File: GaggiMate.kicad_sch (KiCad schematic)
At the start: 26 parts, among them J1 Heater SSR, J13 ESP out, J2 HV_VALVE, J3 K-Type probe, J4 Analog, J5 Pressure Sensor, J6 Brew BTN, J7 Steam BTN, J8 HV_PUMP, J9 HX711 connector, P1 USB_C_Plug_USB2.0, U1 ESP32-S3-WROOM-1, U2 MAX31855KASA, U3 ADS1115IDGS, U4 AMS1117-3.3

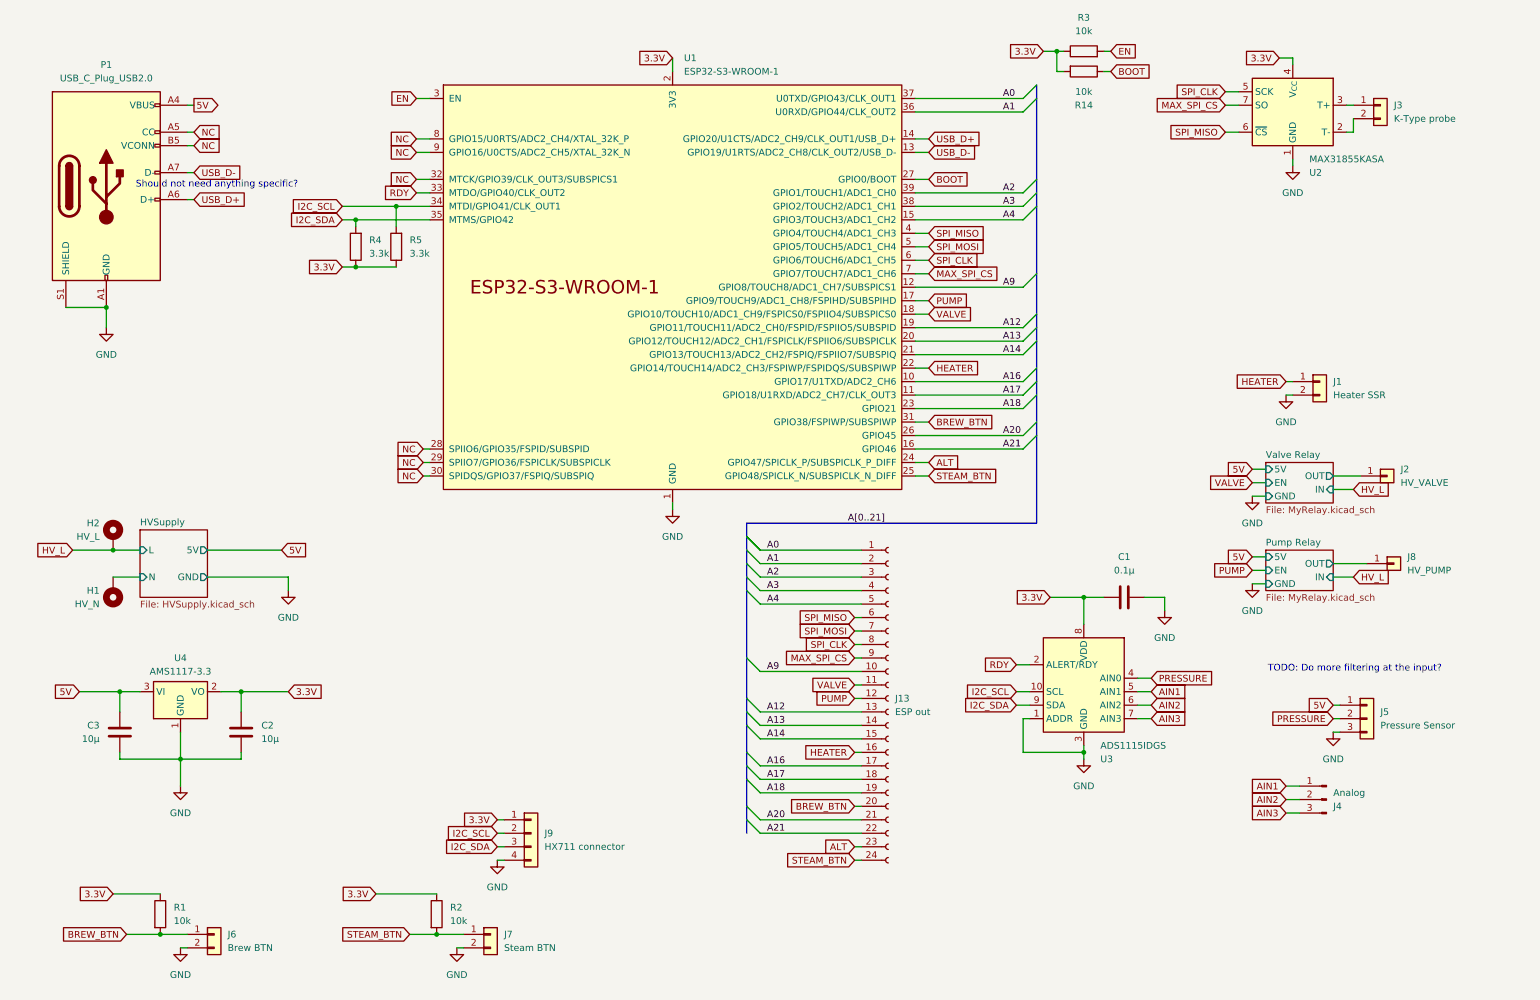
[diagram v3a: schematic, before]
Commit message: update footprints, add 230v module, use SSRs and do some basic layouting
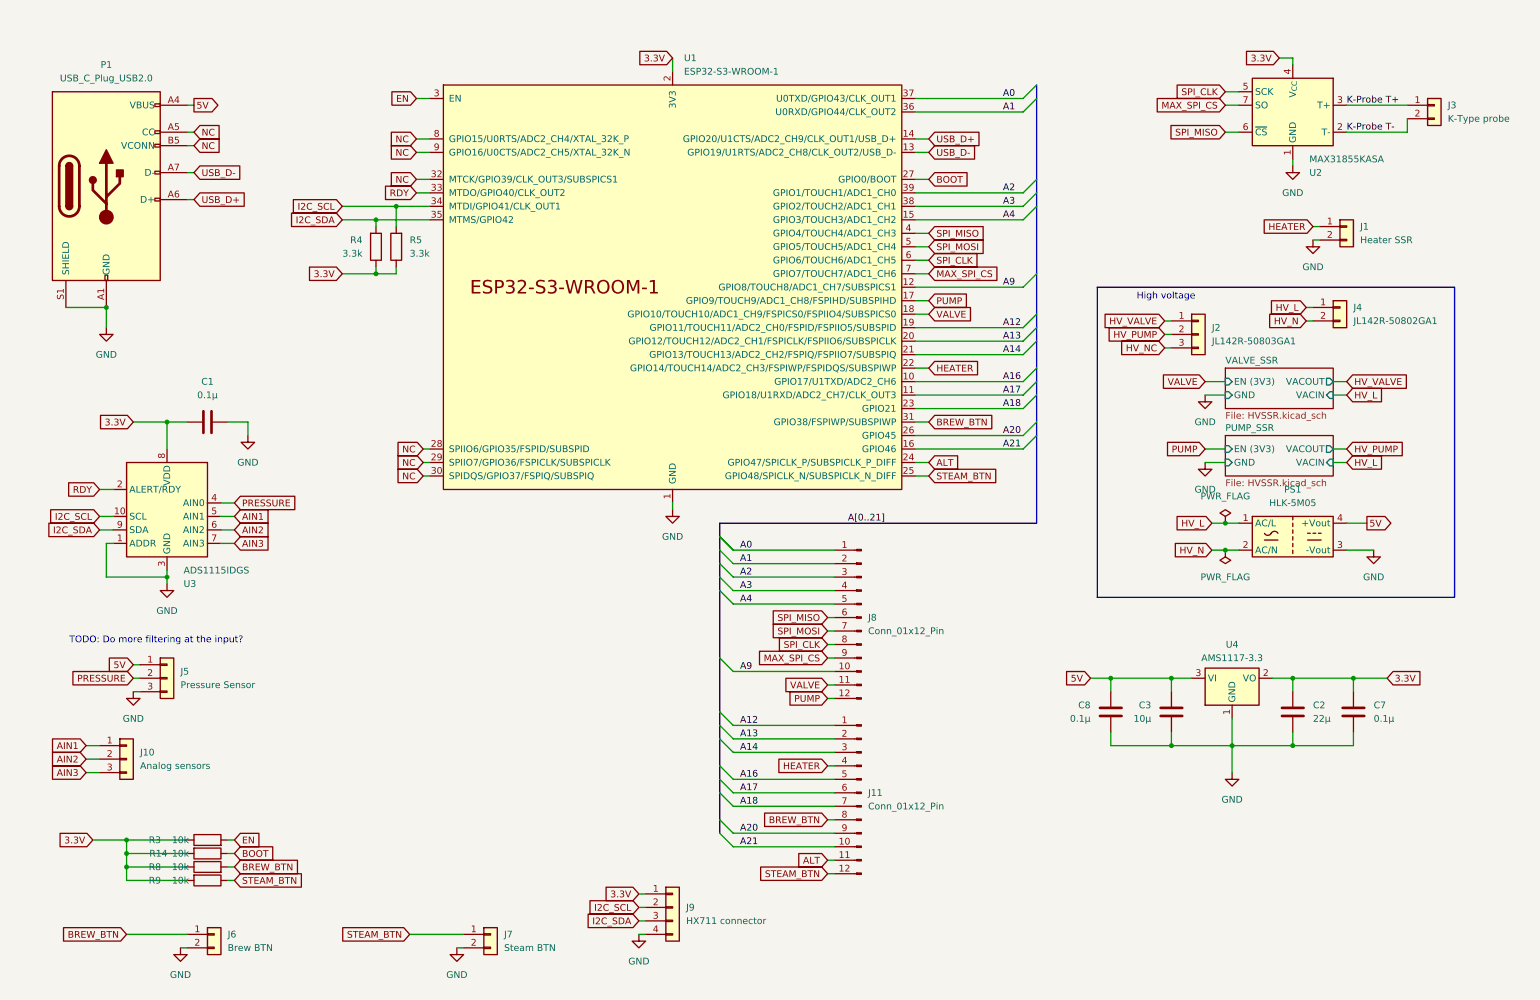
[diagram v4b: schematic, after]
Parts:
- removed H1: HV_N, symbol Mechanical:MountingHole_Pad
- removed H2: HV_L, symbol Mechanical:MountingHole_Pad
- removed J13: ESP out, Connector_PinHeader_2.54mm:PinHeader_1x24_P2.54mm_Vertical_SMD_Pin1Right, symbol Connector:Conn_01x24_Socket
- removed J2: HV_VALVE, symbol Connector_Generic:Conn_01x01
- removed J4: Analog, symbol Connector:Conn_01x03_Pin
- removed J8: HV_PUMP, symbol Connector_Generic:Conn_01x01
- removed R1, R2: 10k, Resistor_SMD:R_0201_0603Metric, symbol Device:R
- added C7, C8: 0.1µ, Capacitor_SMD:C_0201_0603Metric, symbol Device:C
- added J10: Analog sensors, symbol Connector_Generic:Conn_01x03
- added J11, J8: Conn_01x12_Pin, Connector_PinHeader_2.54mm:PinHeader_1x12_P2.54mm_Vertical_SMD_Pin1Left, symbol Connector:Conn_01x12_Pin
- added J2: JL142R-50803GA1, Connector_Phoenix_SPT:PhoenixContact_SPT_2.5_3-V-5.0-EX_1x03_P5.0mm_Vertical, symbol Connector_Generic:Conn_01x03
- added J4: JL142R-50802GA1, Connector_Phoenix_SPT:PhoenixContact_SPT_2.5_2-V-5.0-EX_1x02_P5.0mm_Vertical, symbol Connector_Generic:Conn_01x02
- added PS1: HLK-5M05, Converter_ACDC:Converter_ACDC_Hi-Link_HLK-5Mxx, symbol Converter_ACDC:HLK-5M05
- added R8, R9: 10k, Resistor_SMD:R_0201_0603Metric, symbol Device:R
- C1, C3: footprint (none) -> Capacitor_SMD:C_0201_0603Metric
- C2: value 10µ -> 22µ; footprint (none) -> Capacitor_SMD:C_0201_0603Metric
- J1, J3, J6, J7: footprint (none) -> Connector_JST:JST_PH_B2B-PH-K_1x02_P2.00mm_Vertical
- J5: footprint (none) -> Connector_Phoenix_SPT:PhoenixContact_SPT_2.5_3-V-5.0-EX_1x03_P5.0mm_Vertical
- P1: footprint (none) -> Connector_USB:USB_C_Receptacle_Palconn_UTC16-G
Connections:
- net 3.3V: now also C7.1, R8.1, R9.2
- net 5V: now also C8.2, PS1.4 (+Vout)
- net A0: now also J8.1 (Pin_1)
- net A1: now also J8.2 (Pin_2)
- net A12: now also J11.1 (Pin_1)
- net A13: now also J11.2 (Pin_2)
- net A14: now also J11.3 (Pin_3)
- net A16: now also J11.5 (Pin_5)
- net A17: now also J11.6 (Pin_6)
- net A18: now also J11.7 (Pin_7)
- net A2: now also J8.3 (Pin_3)
- net A20: now also J11.9 (Pin_9)
- net A21: now also J11.10 (Pin_10)
- net A3: now also J8.4 (Pin_4)
- net A4: now also J8.5 (Pin_5)
- net A9: now also J8.10 (Pin_10)
- net AIN1: now also J10.1 (Pin_1)
- net AIN2: now also J10.2 (Pin_2)
- net AIN3: now also J10.3 (Pin_3)
- net ALT: now also J11.11 (Pin_11)
- net BREW_BTN: now also J11.8 (Pin_8), R8.2
- net GND: now also C7.2, C8.1, PS1.3 (-Vout)
- net HEATER: now also J11.4 (Pin_4)
- net HV_L: now also J4.1 (Pin_1), PS1.1 (AC/L)
- net MAX_SPI_CS: now also J8.9 (Pin_9)
- net PUMP: now also J8.12 (Pin_12)
- net SPI_CLK: now also J8.8 (Pin_8)
- net SPI_MISO: now also J8.6 (Pin_6)
- net SPI_MOSI: now also J8.7 (Pin_7)
- net STEAM_BTN: now also J11.12 (Pin_12), R9.1
- net VALVE: now also J8.11 (Pin_11)
- net K-Probe T-: now reaches J3.2 (Pin_2), U2.2 (T-)
- net K-Probe T+: now reaches J3.1 (Pin_1), U2.3 (T+)
- new net HV_N: J4.2 (Pin_2), PS1.2 (AC/N)
- new net HV_NC: J2.3 (Pin_3)
- new net HV_PUMP: J2.2 (Pin_2)
- new net HV_VALVE: J2.1 (Pin_1)
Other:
- removed sheet HVSupply
- removed sheet Pump Relay
- removed sheet Valve Relay
- added sheet PUMP_SSR (HVSSR.kicad_sch)
- added sheet VALVE_SSR (HVSSR.kicad_sch)
- note added: "High voltage"
- note removed: "Should not need anything specific?"
- moved on the sheet: C1, C2, C3, J1, J3, J5, J9, R14, R3, R4, U3, U4

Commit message: update some footprints etc
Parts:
- removed J11: Conn_01x12_Pin, Connector_PinHeader_2.54mm:PinHeader_1x12_P2.54mm_Vertical_SMD_Pin1Left, symbol Connector:Conn_01x12_Pin
- removed J2: JL142R-50803GA1, Connector_Phoenix_SPT:PhoenixContact_SPT_2.5_3-V-5.0-EX_1x03_P5.0mm_Vertical, symbol Connector_Generic:Conn_01x03
- removed J6: Brew BTN, Connector_JST:JST_PH_B2B-PH-K_1x02_P2.00mm_Vertical, symbol Connector_Generic:Conn_01x02
- removed J7: Steam BTN, Connector_JST:JST_PH_B2B-PH-K_1x02_P2.00mm_Vertical, symbol Connector_Generic:Conn_01x02
- added C4: C, Capacitor_SMD:C_0201_0603Metric, symbol Device:C
- added C5: 0.1µ, symbol Device:C
- added C6: 10n, symbol Device:C
- added D1, D2: LED, symbol Device:LED
- added D3: 1N5817, Diode_SMD:D_SOD-123, symbol Diode:1N5817
- added J12: BTNS, Connector_JST:JST_PH_B4B-PH-K_1x04_P2.00mm_Vertical, symbol Connector_Generic:Conn_01x04
- added J2: Conn_01x02, easyeda2kicad:CONN-TH_2P-P5.08_DIBO_DB142V-5.08-2P, symbol Connector_Generic:Conn_01x02
- added J6: Conn_01x10_Pin, symbol Connector:Conn_01x10_Pin
- added R1: 3.3k, Resistor_SMD:R_0201_0603Metric, symbol Device:R
- added R10, R2: 5.1k, Resistor_SMD:R_0201_0603Metric, symbol Device:R
- added R11: 150, Resistor_SMD:R_0201_0603Metric, symbol Device:R
- added R7: 68, Resistor_SMD:R_0201_0603Metric, symbol Device:R
- added U5: USBLC6-2P6, Package_TO_SOT_SMD:SOT-666, symbol Power_Protection:USBLC6-2P6
- J10: footprint (none) -> easyeda2kicad:CONN-TH_3P-P2.54_DIBO_DB141V-2.54-3P
- J3: footprint Connector_JST:JST_PH_B2B-PH-K_1x02_P2.00mm_Vertical -> easyeda2kicad:CONN-TH_2P-P2.54_DIBO_DB141V-2.54-2P
- J4: value JL142R-50802GA1 -> Conn_01x02; footprint Connector_Phoenix_SPT:PhoenixContact_SPT_2.5_2-V-5.0-EX_1x02_P5.0mm_Vertical -> easyeda2kicad:CONN-TH_2P-P5.08_DIBO_DB142V-5.08-2P; now left out of the parts list
- J5: footprint Connector_Phoenix_SPT:PhoenixContact_SPT_2.5_3-V-5.0-EX_1x03_P5.0mm_Vertical -> easyeda2kicad:CONN-TH_3P-P2.54_DIBO_DB141V-2.54-3P
- J8, J9: now not fitted
- PS1: now left out of the parts list
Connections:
- net A16 is gone; now on net A9: U1.10 (GPIO17/U1TXD/ADC2_CH6)
- net A20 is gone; now on net A12: U1.26 (GPIO45)
- net A21 is gone; now on net A13: U1.16 (GPIO46)
- net 3.3V: now also C5.1, D2.2 (A), R1.1
- net 5V: now also D1.2 (A), D3.1 (K); no longer P1.A4 (VBUS), P1.A9 (VBUS), P1.B4 (VBUS), P1.B9 (VBUS)
- net A12: no longer U1.19 (GPIO11/TOUCH11/ADC2_CH0/FSPID/FSPIIO5/SUBSPID)
- net A13: no longer U1.20 (GPIO12/TOUCH12/ADC2_CH1/FSPICLK/FSPIIO6/SUBSPICLK)
- net A9: no longer U1.12 (GPIO8/TOUCH8/ADC1_CH7/SUBSPICS1)
- net ALT: now also J6.10 (Pin_10)
- net BREW_BTN: now also J12.1 (Pin_1), J6.8 (Pin_8)
- net GND: now also C5.2, J12.3 (Pin_3), J12.4 (Pin_4), R11.2, R7.2, U5.2 (GND)
- net HEATER: now also J6.5 (Pin_5)
- net HV_PUMP: now also J2.2 (Pin_2)
- net HV_VALVE: now also J2.1 (Pin_1)
- net K-Probe T+: now also C6.1
- net K-Probe T-: now also C6.2
- net MAX_SPI_CS: now also J6.4 (Pin_4); no longer J8.9 (Pin_9)
- net PUMP: now also J6.7 (Pin_7); no longer J8.12 (Pin_12)
- net RDY: now also R1.2
- net SPI_CLK: now also J6.3 (Pin_3); no longer J8.8 (Pin_8)
- net SPI_MISO: now also J6.1 (Pin_1); no longer J8.6 (Pin_6)
- net SPI_MOSI: now also J6.2 (Pin_2); no longer J8.7 (Pin_7)
- net STEAM_BTN: now also J12.2 (Pin_2), J6.9 (Pin_9)
- net USB_D+: now also U5.4 (I/O2); no longer P1.A6 (D+)
- net USB_D-: now also U5.6 (I/O1); no longer P1.A7 (D-)
- net VALVE: now also J6.6 (Pin_6); no longer J8.11 (Pin_11)
- net A14 renamed A8
- net A8: now also J8.9 (Pin_9)
- net A17 renamed A10
- net A10: now also J8.11 (Pin_11)
- net A18 renamed A11
- net A11: now also J8.12 (Pin_12)
- removed net NC: P1.A5 (CC), P1.B5 (VCONN), U1.28 (SPIIO6/GPIO35/FSPID/SUBSPID), U1.29 (SPIIO7/GPIO36/FSPICLK/SUBSPICLK), U1.30 (SPIDQS/GPIO37/FSPIQ/SUBSPIQ), U1.32 (MTCK/GPIO39/CLK_OUT3/SUBSPICS1), U1.8 (GPIO15/U0RTS/ADC2_CH4/XTAL_32K_P), U1.9 (GPIO16/U0CTS/ADC2_CH5/XTAL_32K_N)
- new net: D2.1 (K), R7.1
- new net: D1.1 (K), R11.1
- new net: C4.1, D3.2 (A), P1.A4 (VBUS), P1.A9 (VBUS), P1.B4 (VBUS), P1.B9 (VBUS), U5.5 (VBUS)
- new net: C4.2, R10.2, R2.2
- new net: P1.A5 (CC), R2.1
- new net: P1.B5 (VCONN), R10.1
- new net: P1.A7 (D-), U5.1 (I/O1)
- new net: P1.A6 (D+), U5.3 (I/O2)
- new net A5: J8.6 (Pin_6), U1.12 (GPIO8/TOUCH8/ADC1_CH7/SUBSPICS1)
- new net A6: J8.7 (Pin_7), U1.19 (GPIO11/TOUCH11/ADC2_CH0/FSPID/FSPIIO5/SUBSPID)
- new net A7: J8.8 (Pin_8), U1.20 (GPIO12/TOUCH12/ADC2_CH1/FSPICLK/FSPIIO6/SUBSPICLK)
- no-connect marks 0 -> 6
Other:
- moved on the sheet: J1, J3, P1, R14, R3, R4, R5, R8, R9, U2
